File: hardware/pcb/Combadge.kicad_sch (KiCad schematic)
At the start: 7 parts, among them U1 NCP160AMX330TBG, U2 ESP32-WROOM-32

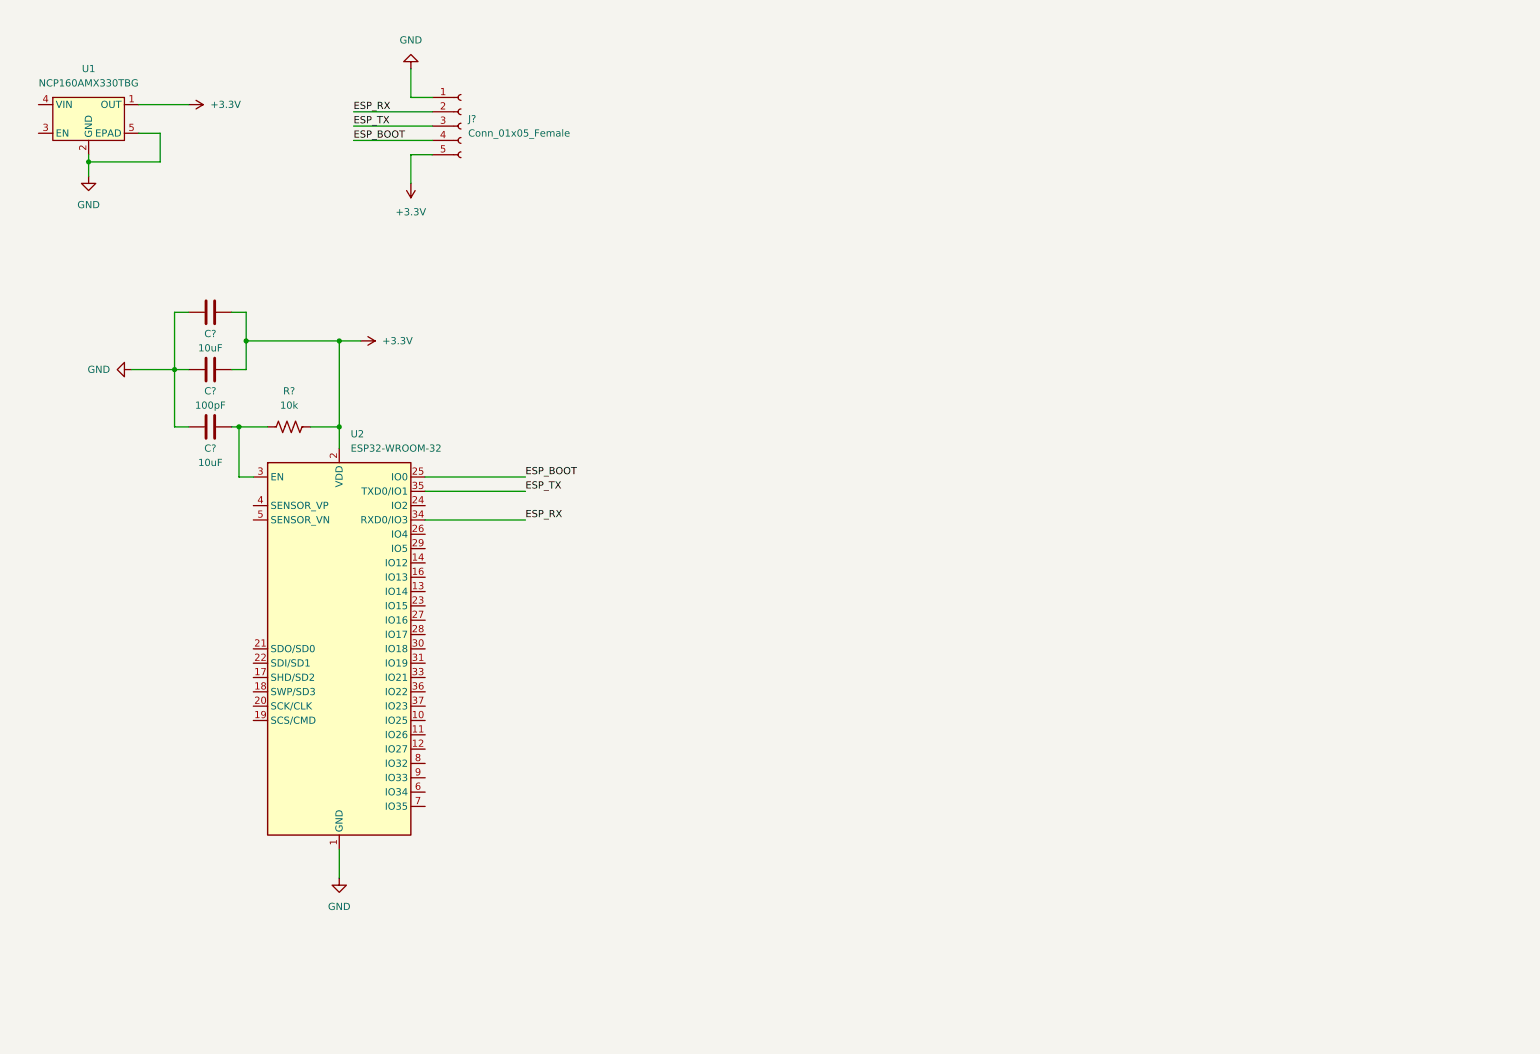
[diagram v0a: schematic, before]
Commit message: Add charging IC to schematic
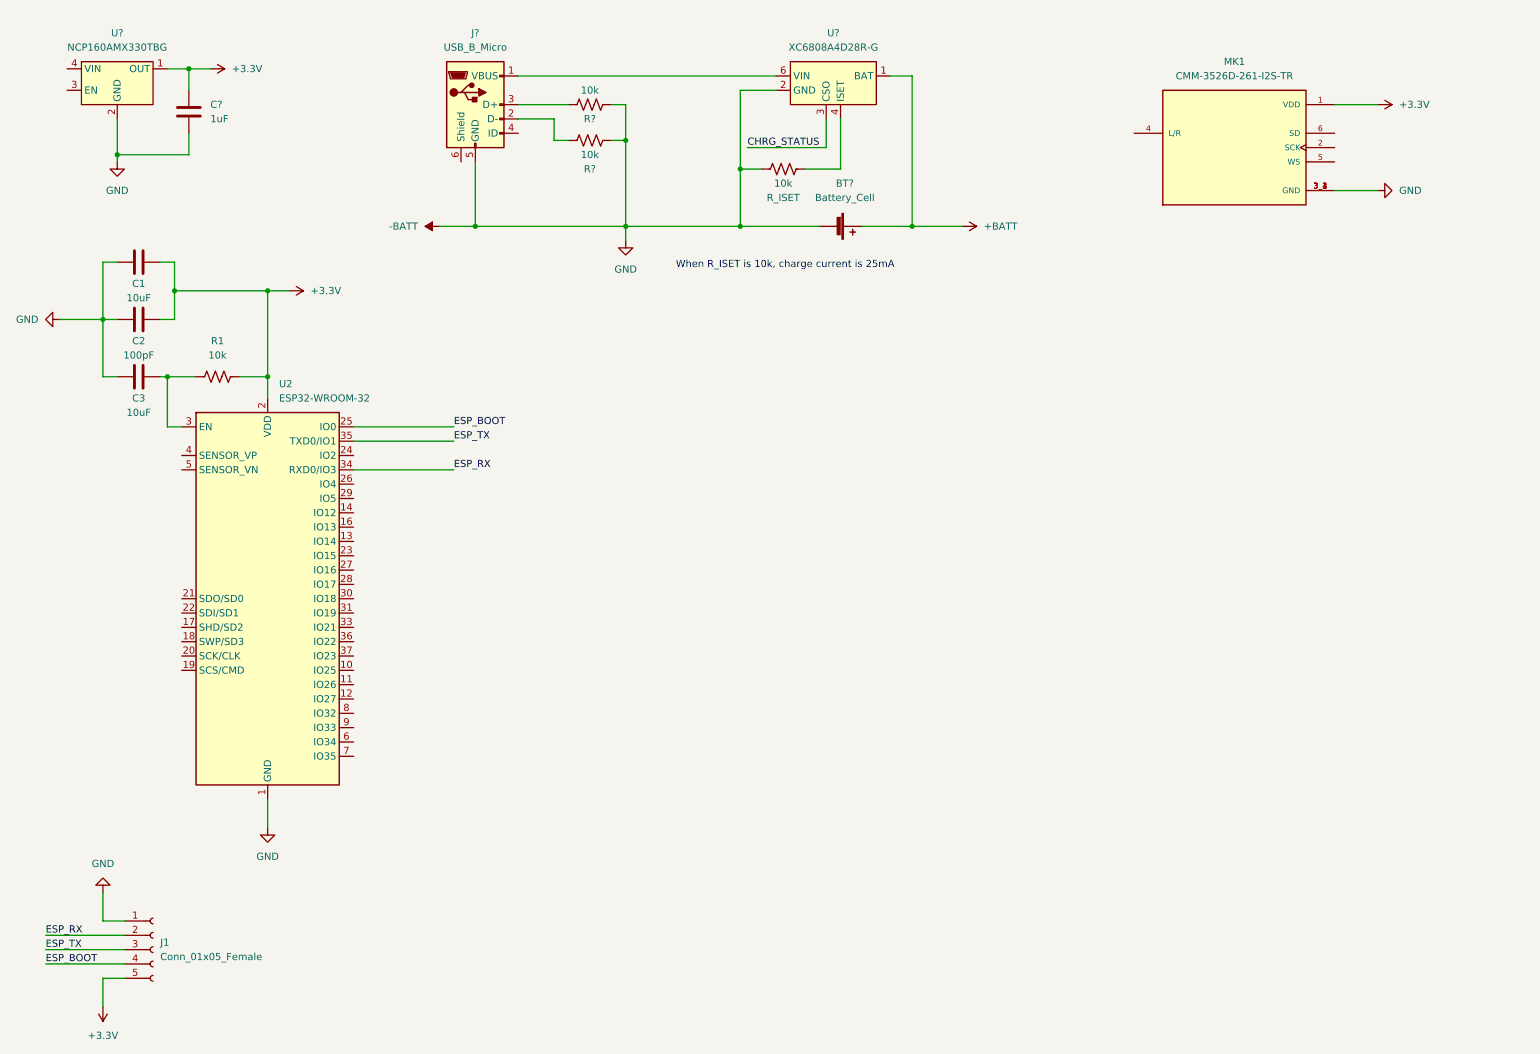
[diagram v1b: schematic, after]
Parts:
- removed U1: NCP160AMX330TBG, Package_DFN_QFN:OnSemi_XDFN4-1EP_1.0x1.0mm_EP0.52x0.52mm, symbol NCP160:NCP160AMX330TBG
- added BT?: Battery_Cell, symbol Device:Battery_Cell
- added C?: 1uF, symbol Device:C
- added J?: USB_B_Micro, symbol Connector:USB_B_Micro
- added MK1: CMM-3526D-261-I2S-TR, MIC_CMM-3526D-261-I2S-TR, symbol CMM-3526D-261-I2S-TR:CMM-3526D-261-I2S-TR
- added R? (x2), R_ISET: 10k, symbol Device:R_US
- added U?: NCP160AMX330TBG, symbol NCP160:NCP160AMX330TBG
- added U?: XC6808A4D28R-G, Torex:USP-6B07, symbol Torex:XC6808A4D28R-G
- gave numbers to parts that had none: 5
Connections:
- net +3.3V: now also C?.1, MK1.1 (VDD), U?.1 (OUT)
- net GND renamed -BATT
- net -BATT: now also BT?.2 (-), C?.2, J?.5 (GND), MK1.3_1 (GND), MK1.3_2 (GND), MK1.3_3 (GND), MK1.3_4 (GND), R?.2, R?.2, R_ISET.1, U?.2 (GND), U?.2 (GND), U?.5 (EPAD)
- new net: R_ISET.2, U?.4 (ISET)
- new net: J?.1 (VBUS), U?.6 (VIN)
- new net: J?.2 (D-), R?.1
- new net: J?.3 (D+), R?.1
- new net +BATT: BT?.1 (+), U?.1 (BAT)
- new net CHRG_STATUS: U?.3 (CSO)
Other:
- note added: "When R_ISET is 10k, charge current is 25mA"
- moved on the sheet: C1, C2, C3, J1, R1, U2

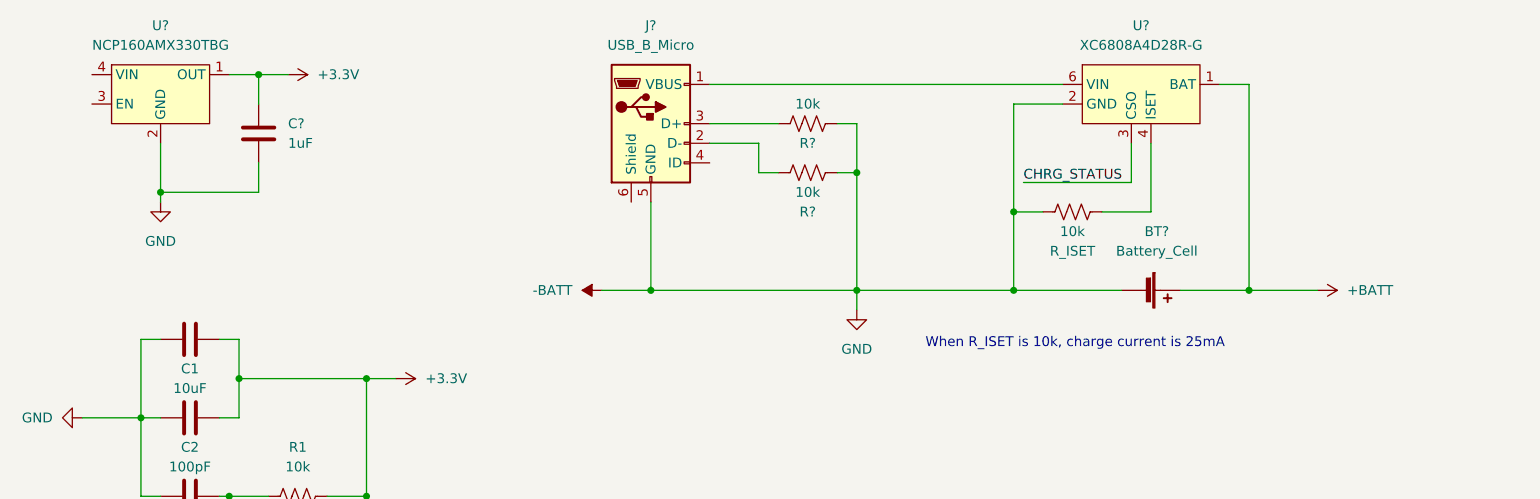
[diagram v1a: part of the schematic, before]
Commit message: Add over-discharge protection circuit
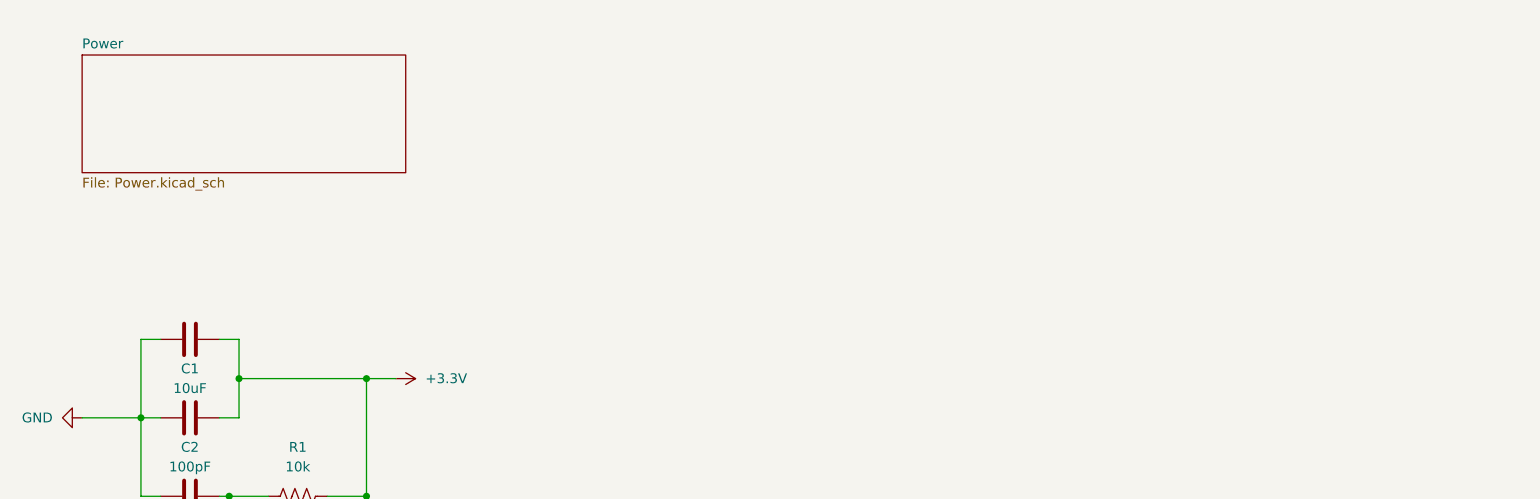
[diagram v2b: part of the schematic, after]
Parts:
- removed BT?: Battery_Cell, symbol Device:Battery_Cell
- removed C?: 1uF, symbol Device:C
- removed J?: USB_B_Micro, symbol Connector:USB_B_Micro
- removed R? (x2), R_ISET: 10k, symbol Device:R_US
- removed U?: NCP160AMX330TBG, symbol NCP160:NCP160AMX330TBG
- removed U?: XC6808A4D28R-G, Torex:USP-6B07, symbol Torex:XC6808A4D28R-G
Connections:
- net -BATT renamed GND
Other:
- added sheet Power (Power.kicad_sch)
- note removed: "When R_ISET is 10k, charge current is 25mA"

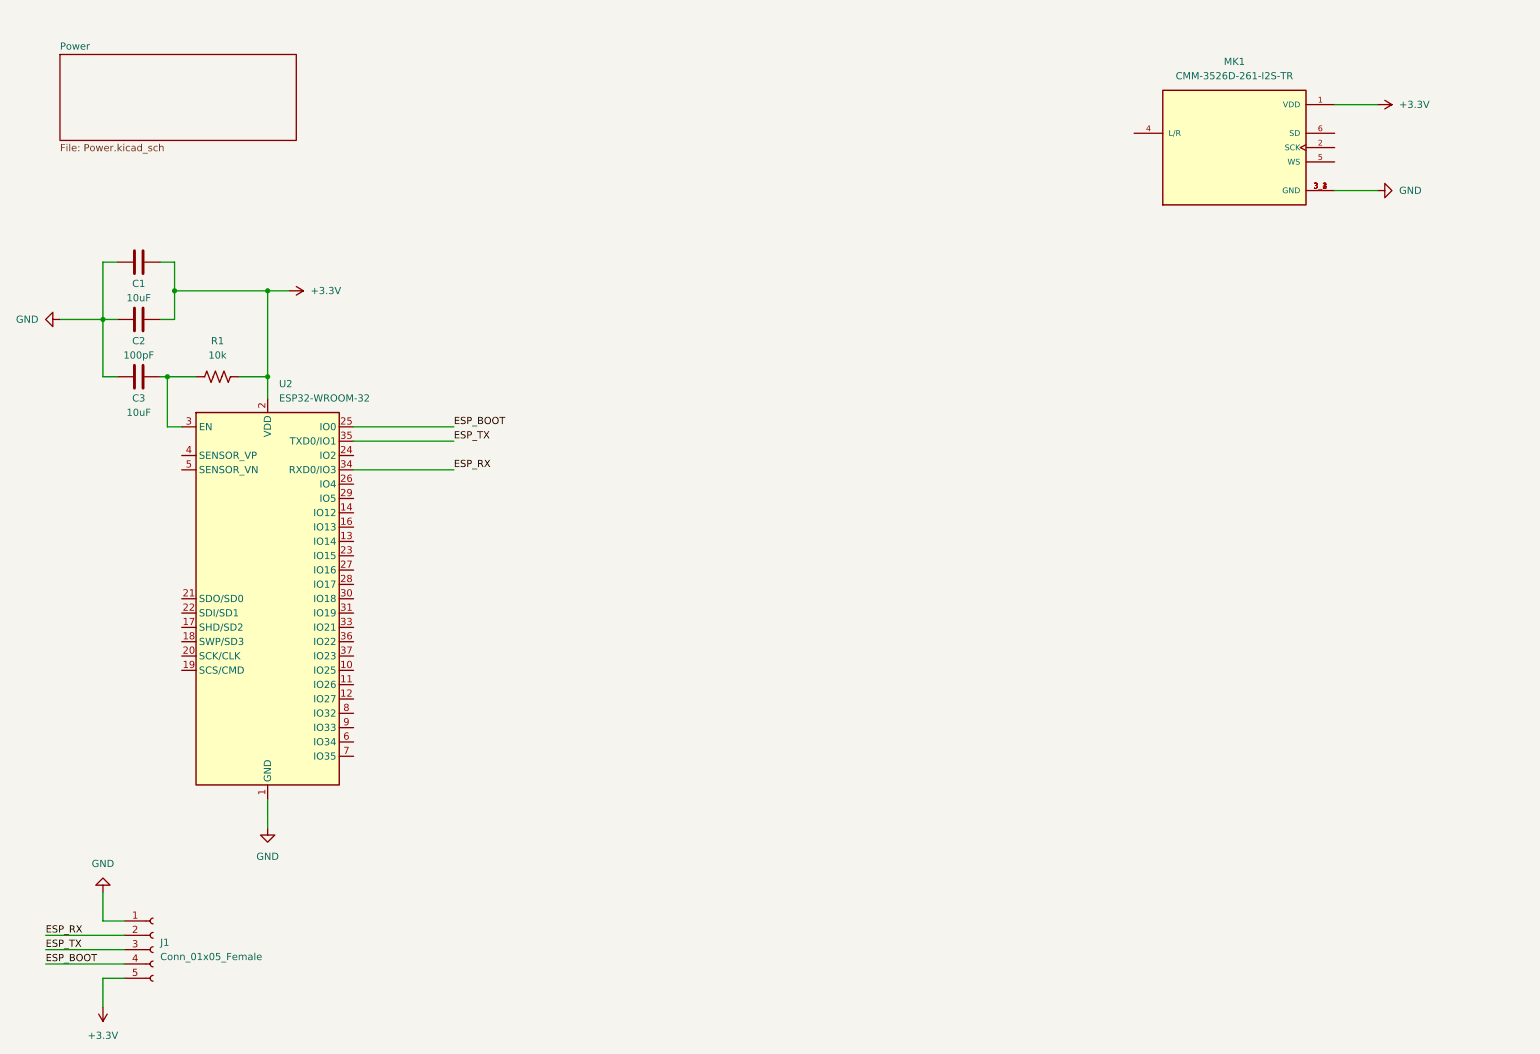
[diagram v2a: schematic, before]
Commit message: Add amplifier to schematic
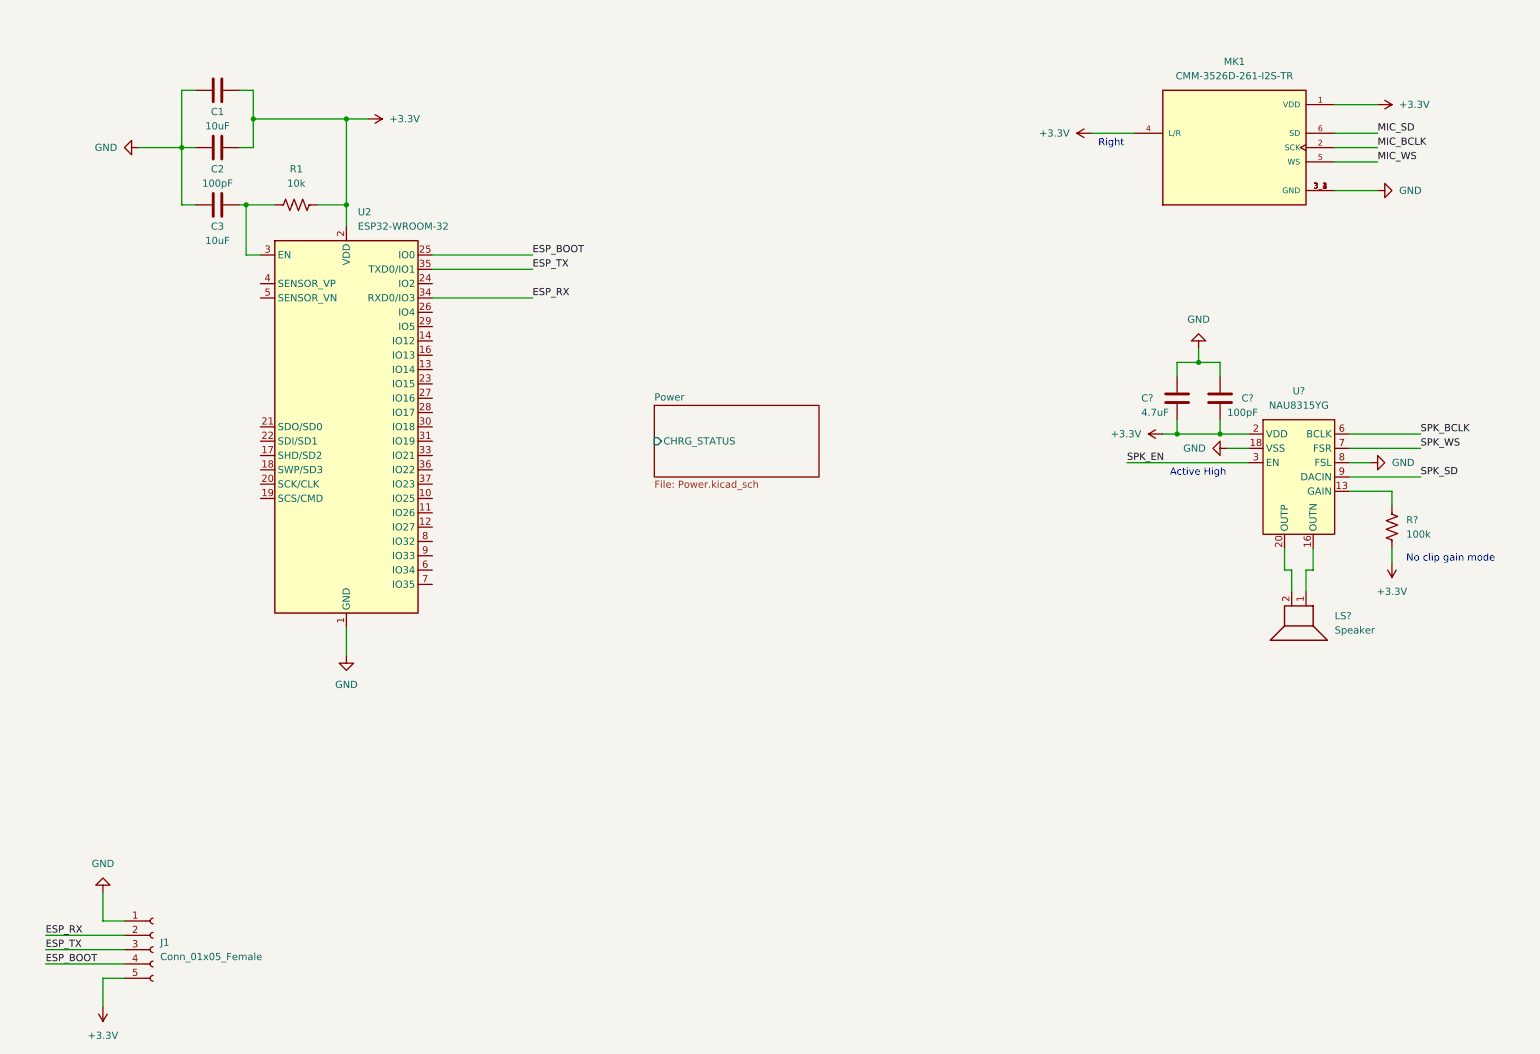
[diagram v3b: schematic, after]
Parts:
- added C?: 4.7uF, symbol Device:C
- added C?: 100pF, symbol Device:C
- added LS?: Speaker, symbol Device:Speaker
- added R?: 100k, symbol Device:R_US
- added U?: NAU8315YG, CustomQFN:QFN-20-1EP_4x4mm_P0.5mm_EP2x2mm, symbol Nuvoton:NAU8315YG
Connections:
- net +3.3V: now also MK1.4 (L/R), C?.2, C?.2, R?.2, U?.11 (VDD), U?.14 (VDD), U?.2 (VDD)
- net GND: now also C?.1, C?.1, U?.12 (VSS), U?.17 (VSS), U?.18 (VSS), U?.19 (VSS), U?.4 (VSS), U?.8 (FSL), U?.Thermal (VSS)
- net MIC_BCLK: now reaches MK1.2 (SCK)
- net MIC_WS: now reaches MK1.5 (WS)
- net MIC_SD: now reaches MK1.6 (SD)
- new net: R?.1, U?.13 (GAIN)
- new net: LS?.1, U?.16 (OUTN)
- new net: LS?.2, U?.20 (OUTP)
- new net: U?.1 (NC), U?.10 (NC), U?.15 (NC), U?.5 (NC)
- new net SPK_BCLK: U?.6 (BCLK)
- new net SPK_EN: U?.3 (EN)
- new net SPK_SD: U?.9 (DACIN)
- new net SPK_WS: U?.7 (FSR)
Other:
- sheet Power ports: added CHRG_STATUS; removed none
- note added: "Active High"
- note added: "No clip gain mode"
- note added: "Right"
- moved on the sheet: C1, C2, C3, R1, U2
